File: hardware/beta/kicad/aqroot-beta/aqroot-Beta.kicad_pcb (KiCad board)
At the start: 4 copper layers, 74 x 155 mm, 188 parts, among them J1 CH280QV10-CT_50P, J2 Molex_5025700893, J3 USB_C_Receptacle_USB2.0_16P, J4 JST-PH-2 BATTERY, J5 COMMUNITY_HEADER_2x13, J6 JST-PH-2 SPEAKER, Q1 AO3400A, SW1 BOOT, SW2 UP, SW3 DOWN, SW4 LEFT, SW5 RIGHT, SW6 A_SELECT, SW7 B_BACK, SW8 HOME, SW9 SW_SPDT, U1 ESP32-S3-WROOM-1, U10 USBLC6-2SC6, U11 BQ25185, U12 TPS63020, U13 TPS61023, U14 MAX17048, U15 TPS22918, U16 TCA9517ADGK, U17 TPS61169DCKR, U2 TCA9535PWR, U3 TCA9535PWR, U4 BMI270, U5 MAX98357A, U6 TSOP38238, U7 E07-400M10S, U8 E22-900M22S, U9 ST25R3916-AQET

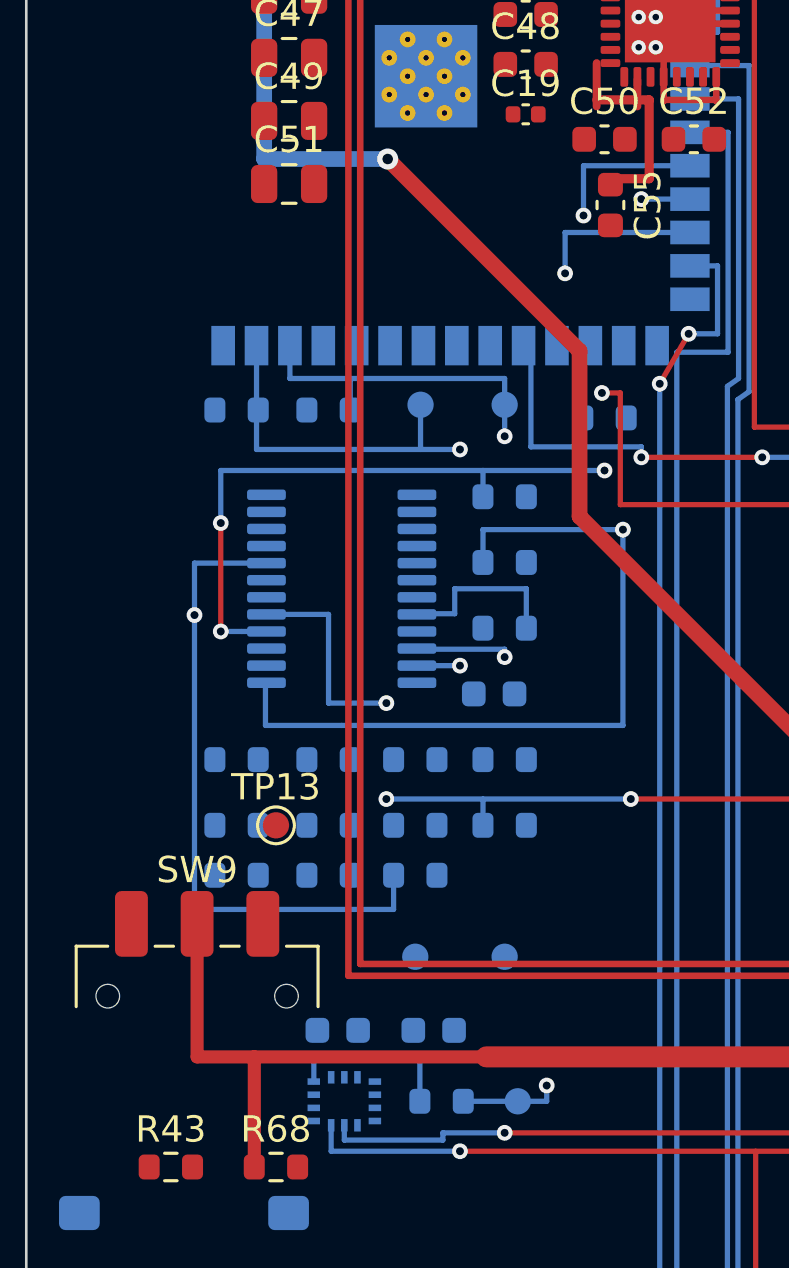
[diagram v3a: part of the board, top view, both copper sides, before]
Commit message: route +3V3 Pass B1 (cluster E normal-width)
Routes 16 of the 17 listed cluster-E pads at ordinary P3V3 geometry:
72.351 mm in 41 tracks and 6 vias across B.Cu 33 / F.Cu 6 / In2 2. Board
ratsnest 384 -> 368, +3V3 ratsnest 48 -> 32, +3V3 islands 49 -> 33, source
island 27 -> 43 pads. DRC 0 electrical errors.

NO E6 RELIEF WAS USED. Every B1 track is 0.60 mm (27) or 0.40 mm (14) - all at
or above the P3V3 outer-layer minimum - and every via is POWER-class 0.80/0.40.
The whole pass stays legal with all E6 rules conceptually ignored: no width
below 0.40 and no clearance relief anywhere. Minimum clearance is 0.2000 mm,
the ordinary global figure.

Routed in three geographic batches, DRC 0 after each: A, the U2 area and west
pull-up bank (U2.24, C4.1, R7.1, R6.1, R5.1, R4.1, R10.1, R9.1, R8.1); B, the
BMI270 normal pads and local decoupling (U4.8, U4.3, U4.2, C7.1, C6.1); C, the
north pull-ups (R20.1, R19.1). U4.8 is the real BMI270 VDD supply and takes the
short direct 0.40 mm feed; U4.2 and U4.3 are auxiliary-interface straps.

C13.1 IS DEFERRED TO B2, and this is the one item of the brief's B1 list left
open. It sits mid-board at (29.275,79.000), not in the west bank, and cannot
reach the source island on its own within the search bound. Its natural feed is
the cluster G/H branch that B2 builds - the C43/L3 island B2 absorbs sits
3.9 mm away at (34.5,83.15), while the nearest source-island copper is roughly
26 mm north. Routing it in B1 is possible only by attaching it to that orphan
island, which would leave it off the source island entirely; an earlier attempt
did exactly that and the connectivity audit caught it. Deferring one pad to the
adjacent pass is the correct call rather than forcing a long private feed.

Two defects in the first attempt were found and fixed before anything was
committed. The tree seed was taken from every +3V3 segment on the board rather
than from the source island alone, which let C13.1 attach to the unabsorbed
C43/L3 island; the seed is now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
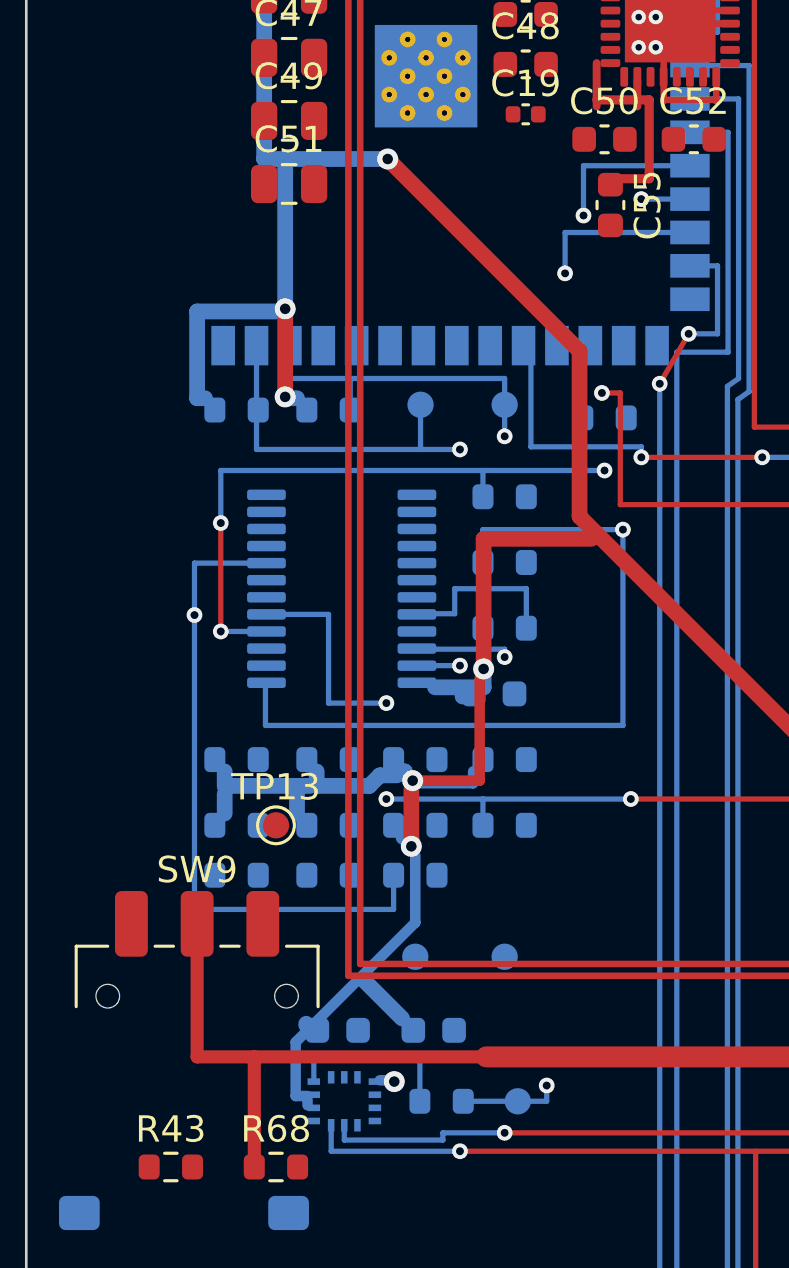
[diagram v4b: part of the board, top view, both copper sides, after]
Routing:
- net +3V3: track 281.2 -> 353.5 mm, vias 13 -> 19

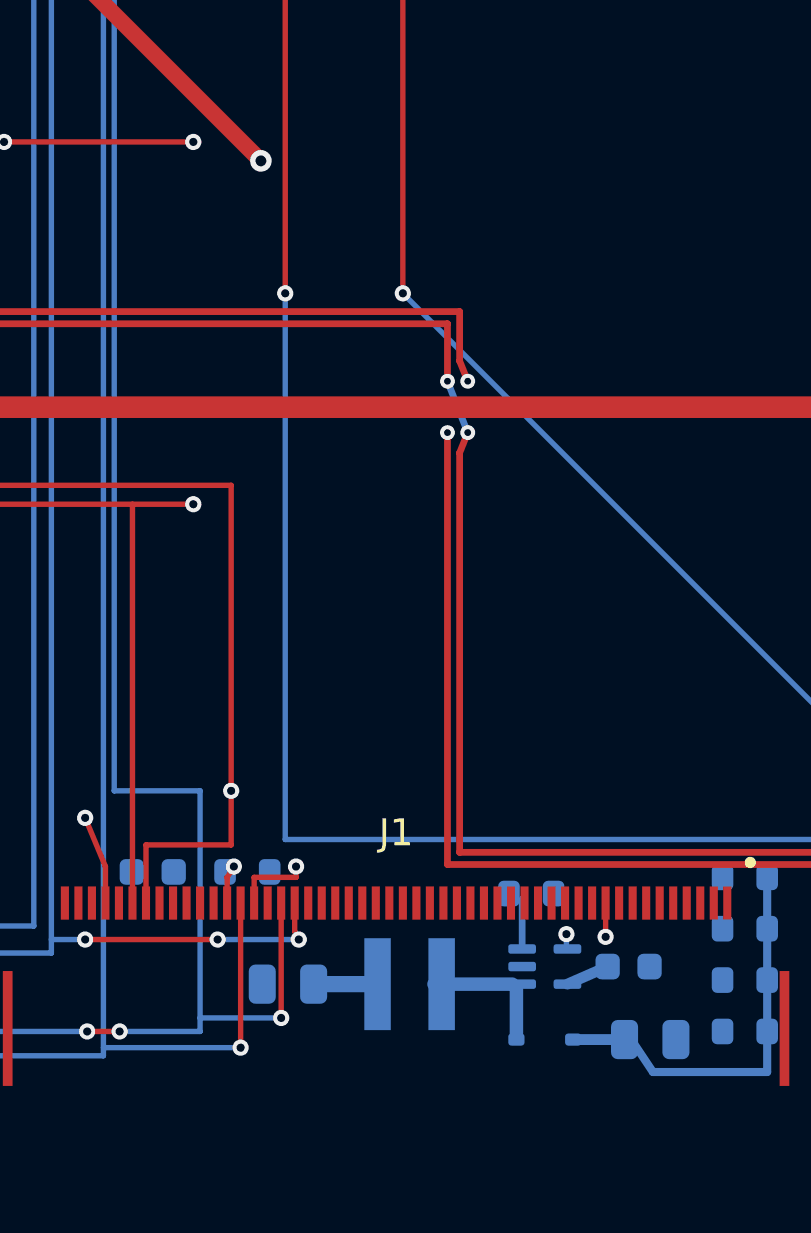
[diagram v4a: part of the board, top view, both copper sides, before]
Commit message: route +3V3 Pass B2 (cluster G, cluster H absorption, C13.1)
Absorbs both orphan cluster-H islands, routes the normal-width cluster-G pads
and closes C13.1: 53.140 mm in 17 tracks and 3 vias across B.Cu 13 / F.Cu 4.
Board ratsnest 368 -> 361, +3V3 ratsnest 32 -> 25, +3V3 islands 33 -> 26,
source island 43 -> 52 pads. DRC 0 electrical errors.

All nine B2 pads - J1.7, J1.8, J1.9, R26.1, C43.1, L3.1, C56.1, U17.5 and
C13.1 - are on the one island containing U12.4/U12.5.

NO E6 RELIEF WAS USED. Widths are 0.60 mm (12) and 0.50 mm (5), all at or above
the P3V3 outer minimum, and no B2 segment enters any of the 13 relief pockets at
all. The pass stays legal with every E6 rule conceptually ignored. Minimum
clearance is 0.2000 mm, the ordinary global figure. All three vias are
POWER-class 0.80/0.40.

The tree seed was recomputed from scratch after every single route, seeding only
from the verified source island containing U12.4 - the standing rule introduced
after the B1 bug. Each step re-verified membership before the next began, and
every line of the build log carries its own SOURCE-CONNECTED confirmation.

Substeps, DRC 0 after each:

  A  H1, the C43/L3 island, absorbed with a 32.200 mm 0.60 mm B.Cu run south
     from the Pass-A backbone at (32.550,53.050) to (36.350,81.450).
  B  H2, the C56/U17 island, absorbed with 12.100 mm teed off the now
     source-connected H1 branch rather than from the source directly.
  C  cluster G: J1.9 (2.190 mm) and J1.7 (0.250 mm) at 0.50 mm; J1.8 and
     R26.1 came in on those same branches.
  D  C13.1 closed with a short 6.400 mm local feed off the mid-board branch.

C13.1 was the pad deferred from B1, and this is exactly why. Its feed is
6.400 mm from the now source-connected G/H branch, against roughly 26 mm for a
private run from the source - the long private feed B1 was told not to create.
The B1 failure mode is also excluded by construction here: the H islands were
joined to the source and verified BEFORE C13.1 was routed, so C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
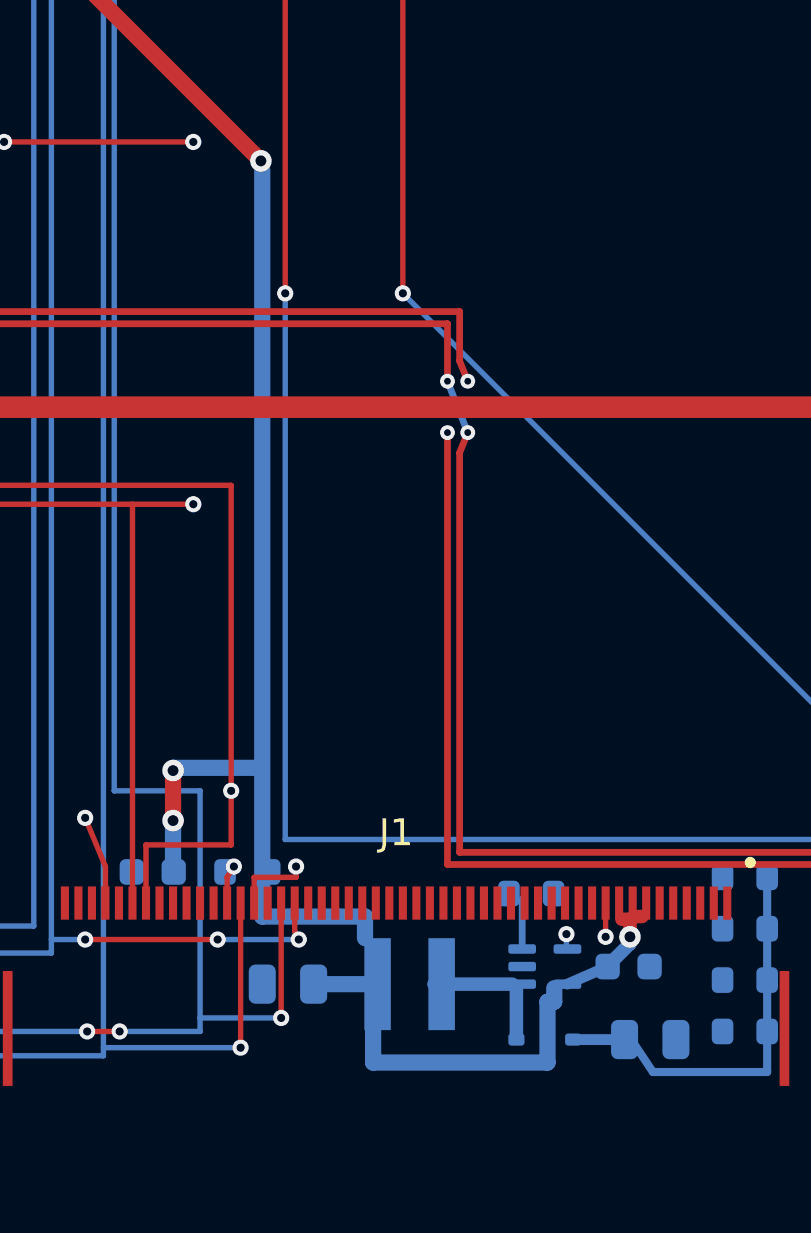
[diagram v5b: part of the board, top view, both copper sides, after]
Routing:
- net +3V3: track 353.5 -> 406.6 mm, vias 19 -> 22
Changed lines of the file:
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@@
+	)
+	(segment
+		(start 46.15 81.4)
+		(end 46.15 80.75)
+		(width 0.5)
+		(layer "F.Cu")
+		(net "+3V3")
+	)
+	(segment
+		(start 46.15 80.75)
+		(end 45.85 80.75)
+		(width 0.5)
+		(layer "F.Cu")
+		(net "+3V3")
+	)
+	(segment
+		(start 46.35 80.65)
+		(end 46.6 80.65)
+		(width 0.5)
+		(layer "F.Cu")
+		(net "+3V3")
+	)
+	(segment
+		(start 29.25 75.25)
+		(end 29.25 77.1)
+		(width 0.6)
+		(layer "F.Cu")
+		(net "+3V3")
 	)
 	(segment
@@
 	)
 	(via
+		(at 46.15 81.4)
+		(size 0.8)
+		(drill 0.4)
+		(layers "F.Cu" "B.Cu")
+		(net "+3V3")
+	)
+	(via
+		(at 29.25 75.25)
+		(size 0.8)
+		(drill 0.4)
+		(layers "F.Cu" "B.Cu")
+		(net "+3V3")
+	)
+	(via
+		(at 29.25 77.1)
+		(size 0.8)
+		(drill 0.4)
+		(layers "F.Cu" "B.Cu")
+		(net "+3V3")
+	)
+	(via
 		(at 65.75 54.4)
 		(size 0.8)
@@
 		(width 0.6)
 		(layer "B.Cu")
+		(net "+3V3")
+	)
+	(segment
+		(start 32.55 53.05)
+		(end 32.55 80.65)
+		(width 0.6)
+		(layer "B.Cu")
+		(net "+3V3")
+	)
+	(segment
+		(start 32.55 80.65)
+		(end 36.35 80.65)
+		(width 0.6)
+		(layer "B.Cu")
+		(net "+3V3")
+	)
+	(segment
+		(start 36.35 80.65)
+		(end 36.35 81.45)
+		(width 0.6)
+		(layer "B.Cu")
+		(net "+3V3")
+	)
+	(segment
+		(start 36.65 83.4)
+		(end 36.65 86.05)
+		(width 0.6)
+		(layer "B.Cu")
+		(net "+3V3")
+	)
+	(segment
+		(start 36.65 86.05)
+		(end 43.1 86.05)
+		(width 0.6)
+		(layer "B.Cu")
+		(net "+3V3")
+	)
+	(segment
+		(start 43.1 86.05)
+		(end 43.1 83.8)
+		(width 0.6)
+		(layer "B.Cu")
+		(net "+3V3")
+	)
+	(segment
+		(start 43.1 83.8)
+		(end 43.35 83.8)
+		(width 0.6)
+		(layer "B.Cu")
+		(net "+3V3")
+	)
+	(segment
+		(start 43.35 83.8)
+		(end 43.35 83.3)
+		(width 0.6)
+		(layer "B.Cu")
+		(net "+3V3")
+	)
+	(segment
+		(start 45.45 82.35)
+		(end 46.15 81.65)
+		(width 0.5)
+		(layer "B.Cu")
+		(net "+3V3")
+	)
+	(segment
+		(start 46.15 81.65)
+		(end 46.15 81.4)
+		(width 0.5)
+		(layer "B.Cu")
+		(net "+3V3")
+	)
+	(segment
+		(start 32.25 75.15)
+		(end 29.25 75.15)
+		(width 0.6)
+		(layer "B.Cu")
+		(net "+3V3")
+	)
+	(segment
+		(start 29.25 75.15)
+		(end 29.25 75.25)
+		(width 0.6)
+		(layer "B.Cu")
+		(net "+3V3")
+	)
+	(segment
+		(start 29.25 77.1)
+		(end 29.25 78.55)
+		(width 0.6)
+		(layer "B.Cu")
